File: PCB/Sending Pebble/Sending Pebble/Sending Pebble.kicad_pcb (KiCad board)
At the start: 4 copper layers, 50 x 50 mm, 48 parts, among them J1 USB_C_Receptacle_USB2.0_16P, J2 Conn_01x02_Socket, J3 u.Fl, J4 SMA, J5 Conn_01x02_Socket, Q1 IRLML0030, SW1 Boot, SW2 Reset, U1 LoRa-E5, U3 MAX-M10S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

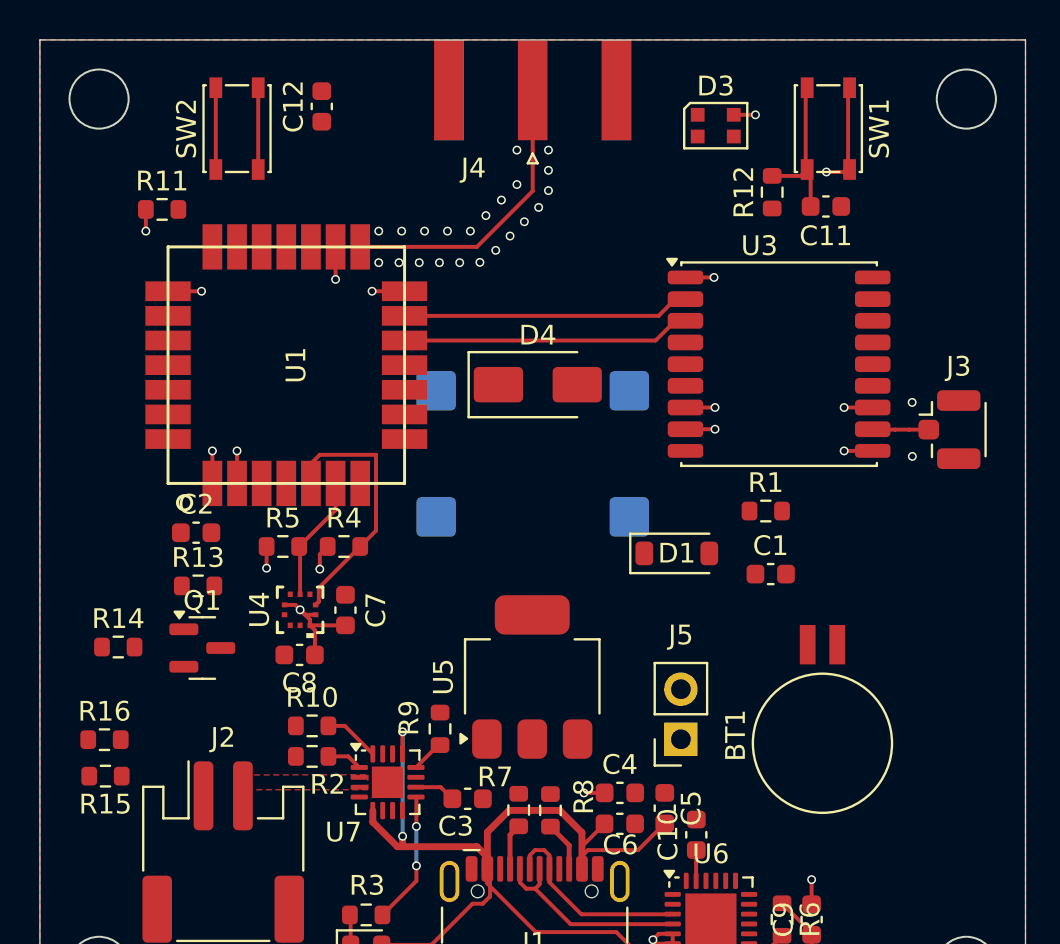
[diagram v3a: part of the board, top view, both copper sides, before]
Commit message: More layout and trace routing
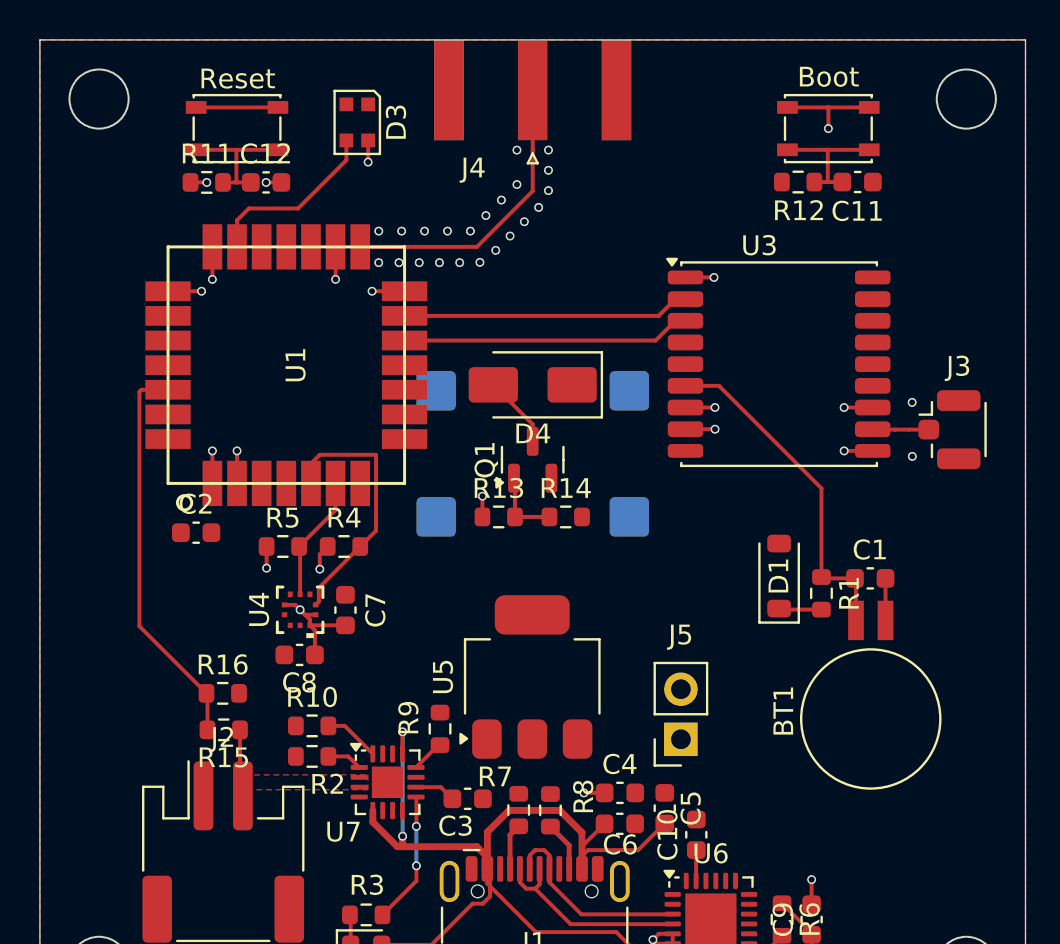
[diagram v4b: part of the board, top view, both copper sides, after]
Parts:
- moved R14 23.6 mm to (138.6, 81.8)
- moved Q1 19.3 mm to (136.9, 78.9), turned to 90 degrees
- moved D3 18.2 mm to (128.0, 61.8), turned to -90 degrees
- moved R13 15.6 mm to (135.2, 81.8)
- moved R15 6.44 mm to (121.2, 92.6)
- moved R16 6.44 mm to (121.2, 90.8)
- moved D1 5.32 mm to (149.4, 84.8), turned to 90 degrees
- moved C1 5.05 mm to (154.0, 84.9)
- moved R1 5.04 mm to (151.6, 85.7), turned to -90 degrees
- moved C12 4.78 mm to (123.4, 64.8), turned to 0 degrees
- moved BT1 2.74 mm to (154.1, 87.0)
- moved R11 2.65 mm to (120.4, 64.8)
- moved C11 2.03 mm to (153.4, 64.8)
- moved R12 1.41 mm to (150.4, 64.8), turned to 0 degrees
- moved D4 0.26 mm to (136.9, 75.1), turned to 180 degrees
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- renumbered SW1 to Boot, SW2 to Reset
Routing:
- net ADC: track 0.00 -> 20.1 mm
- net Net-(BT1-+): track 0.00 -> 17.4 mm
- net NEO: track 0.00 -> 9.16 mm
- net Net-(Q1-G): track 0.00 -> 3.73 mm
- net Net-(BZ1--): track 0.00 -> 3.69 mm
- net Net-(J2-Pin_2): track 0.00 -> 3.41 mm
- net RST: track 4.15 -> 7.22 mm
- net GND: track 16.4 -> 19.3 mm, vias 32 -> 33
- net BUZZ: track 0.00 -> 2.70 mm, vias 0 -> 2
- net Net-(D1-K): track 0.00 -> 2.17 mm
- net BOOT0: track 7.91 -> 7.21 mm

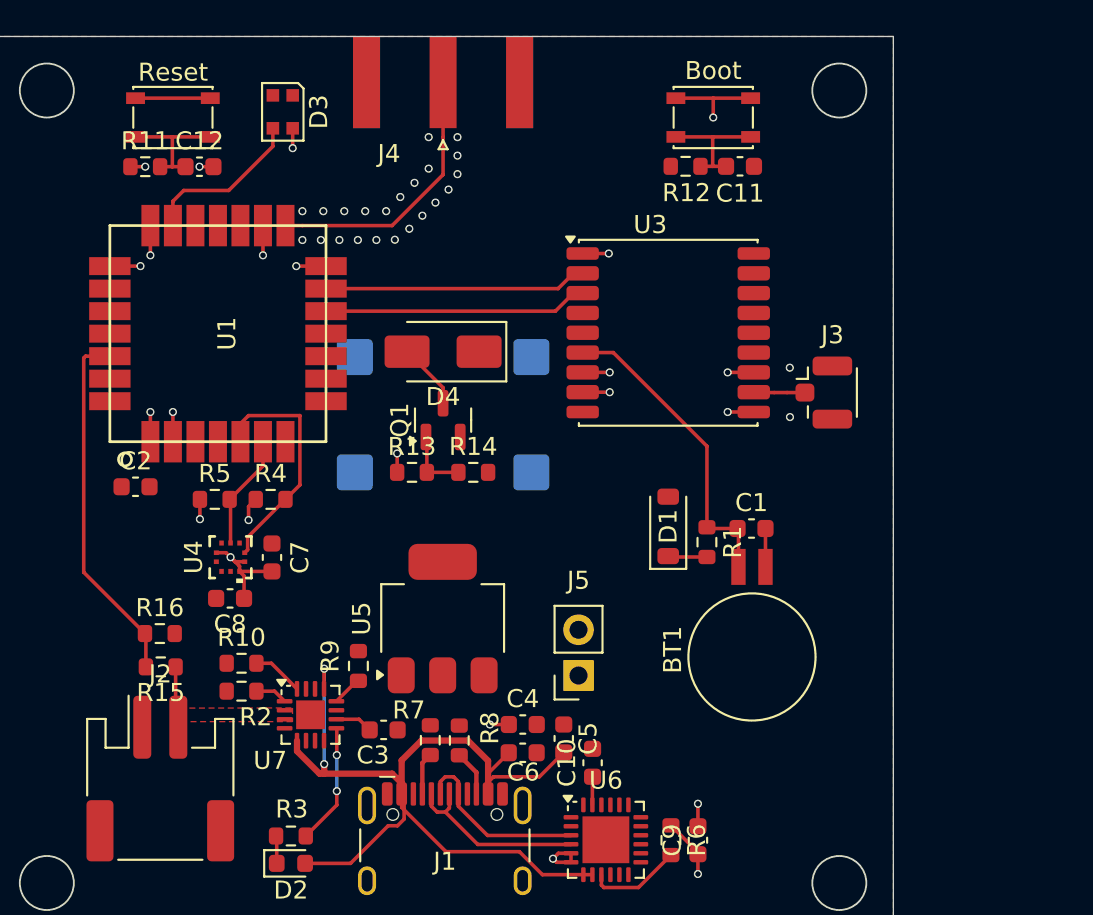
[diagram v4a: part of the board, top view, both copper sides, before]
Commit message: Fixed VREG type, more routing
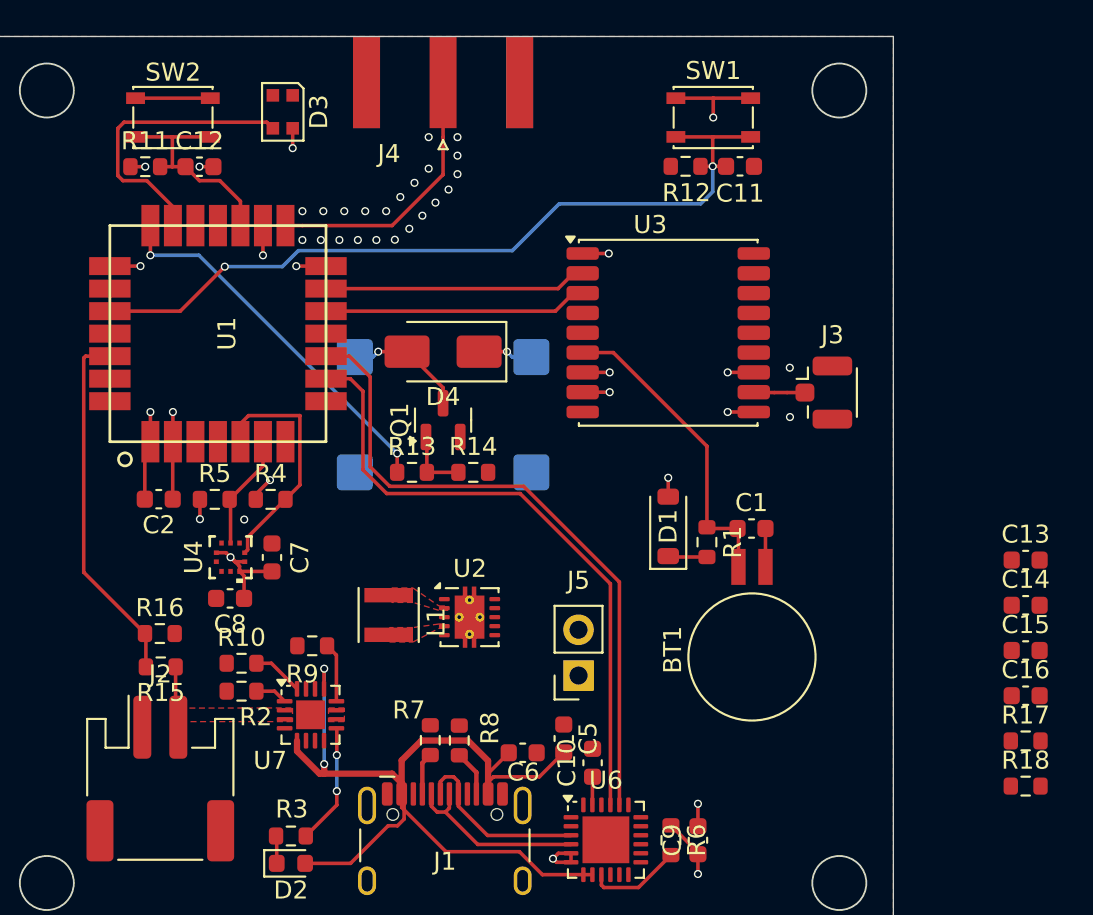
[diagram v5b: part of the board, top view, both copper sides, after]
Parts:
- removed C3: 10uF, Capacitor_SMD:C_0603_1608Metric
- removed C4: 22uF, Capacitor_SMD:C_0603_1608Metric
- removed U5: AZ1117CH2-3.3, Package_TO_SOT_SMD:SOT-223-3_TabPin2
- added C13: 10uF, Capacitor_SMD:C_0603_1608Metric, F.Cu at (169.2, 86.7)
- added C14: 10uF, Capacitor_SMD:C_0603_1608Metric, F.Cu at (169.2, 89.2)
- added C15: 0.1uF, Capacitor_SMD:C_0603_1608Metric, F.Cu at (169.2, 91.7)
- added C16: 10uF, Capacitor_SMD:C_0603_1608Metric, F.Cu at (169.2, 94.2)
- added L1: L, LQH3NPN2R2MMEL:IND_LQH3NPN2R2MMEL, F.Cu at (133.9, 89.7)
- added R17: 100, Resistor_SMD:R_0603_1608Metric, F.Cu at (169.2, 96.7)
- added R18: 10k, Resistor_SMD:R_0603_1608Metric, F.Cu at (169.2, 99.2)
- added U2: TPS63001, Package_SON:Texas_DRC0010J_ThermalVias, F.Cu at (138.4, 89.8)
- moved R9 2.80 mm to (129.6, 91.4), turned to 0 degrees
- moved C2 1.46 mm to (121.1, 83.3), turned to 180 degrees
- renumbered Boot to SW1, Reset to SW2
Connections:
- J5 pad 1: VBAT -> Net-(J5-Pin_1)
- J5 pad 2: Net-(J5-Pin_2) -> VBAT
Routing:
- net BOOT0: track 7.21 -> 44.8 mm, vias 0 -> 2
- net PB6/TX: track 0.00 -> 36.8 mm
- net PB7/RX: track 0.00 -> 35.3 mm
- net BUZZ: track 2.70 -> 21.0 mm
- net NEO: track 9.16 -> 16.3 mm
- net +3.3V: track 27.5 -> 33.9 mm, vias 12 -> 13
- net RST: track 7.22 -> 12.4 mm
- net GND: track 19.3 -> 22.5 mm, vias 33 -> 34
- net Net-(BZ1--): track 3.69 -> 6.72 mm, vias 0 -> 1
- net VBAT: track 2.11 -> 0.00 mm
- net Net-(U7-ILIM): track 1.69 -> 3.29 mm
- added copper zone on F.Cu, net Net-(U2-L1)
- added copper zone on F.Cu, net Net-(U2-L2)
- added copper zone on F.Cu, net VBAT

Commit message: More routing, added FC connection
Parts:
- moved C14 31.1 mm to (138.4, 85.5), turned to 180 degrees
- moved R17 31.1 mm to (138.4, 92.6)
- moved C13 30.9 mm to (138.4, 87.1), turned to 180 degrees
- moved C16 30.8 mm to (138.4, 94.2), turned to 180 degrees
- moved C15 27.7 mm to (141.6, 88.9), turned to 90 degrees
- moved R18 14.6 mm to (155.0, 96.5), turned to -90 degrees
- moved D3 14.1 mm to (115.0, 67.3), turned to 0 degrees
- moved PWR0 13.4 mm to (157.6, 95.6)
- moved R15 6.67 mm to (116.9, 87.5)
- moved R16 6.67 mm to (116.8, 85.7)
- moved J2 4.12 mm to (119.1, 95.2), turned to -90 degrees
- moved C1 3.73 mm to (151.4, 82.3)
- moved BT1 3.73 mm to (151.4, 84.4)
- moved D1 3.73 mm to (146.7, 82.2)
- moved R1 3.73 mm to (148.9, 83.1)
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- renumbered SW1 to BOOT, J5 to PWR0, SW2 to RESET
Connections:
- PWR0 pad 1: Net-(J5-Pin_1) -> EN
- R18 pad 1: Net-(J5-Pin_1) -> EN
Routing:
- net RST: track 12.4 -> 52.5 mm, vias 0 -> 2
- net VBAT: track 0.00 -> 23.7 mm, vias 0 -> 1
- net EN: track 0.00 -> 22.8 mm, vias 0 -> 1
- net NEO: track 16.3 -> 7.69 mm
- net Net-(J2-Pin_2): track 3.41 -> 11.5 mm
- net Net-(U2-PS/SYNC): track 0.00 -> 6.92 mm
- net ADC: track 20.1 -> 14.0 mm
- net +3.3V: track 33.9 -> 39.0 mm, vias 13 -> 15
- net GND: track 22.5 -> 26.7 mm, vias 34 -> 41
- net Net-(BT1-+): track 17.4 -> 14.1 mm
- net BOOT0: track 44.8 -> 42.1 mm
- net Net-(U7-TS): track 1.80 -> 3.71 mm
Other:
- outline, holes or cut-outs redrawn

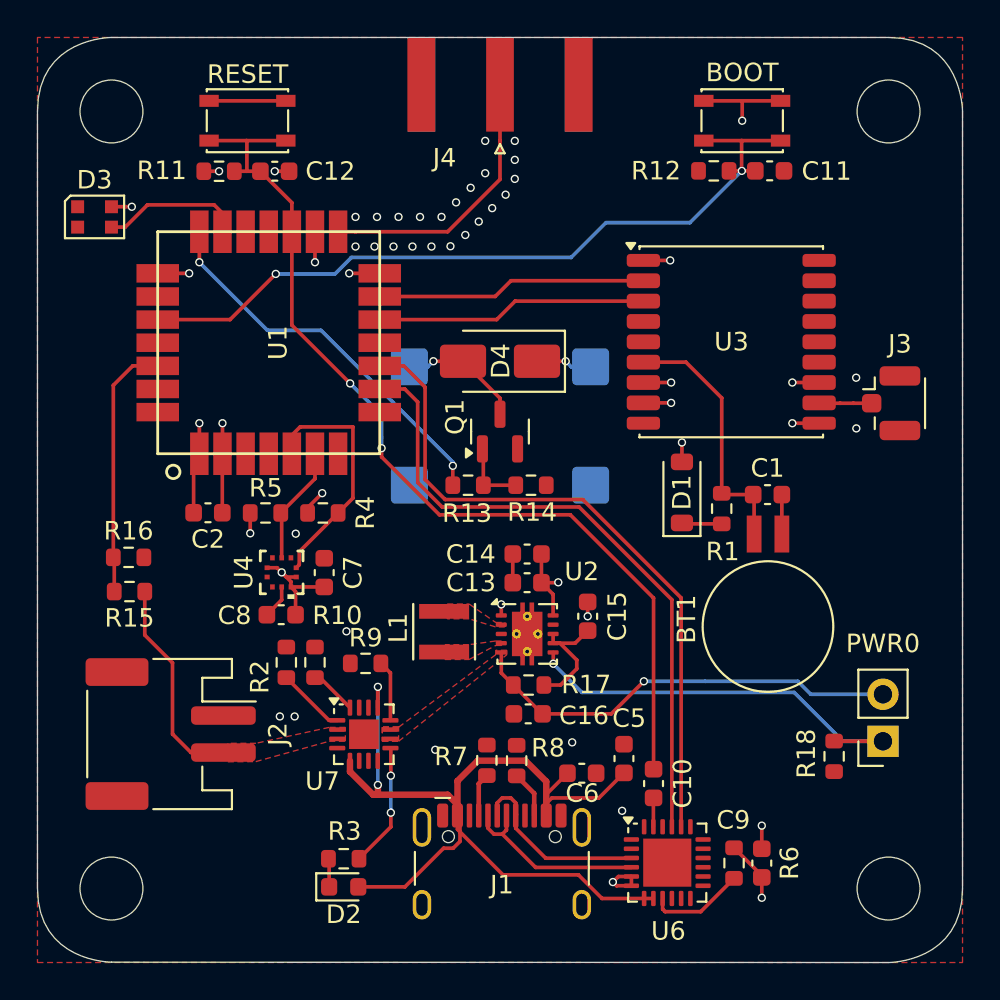
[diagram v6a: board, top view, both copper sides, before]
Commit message: More routing, added amplifier connector, fixed coplanar waveguide. Started adding graphics
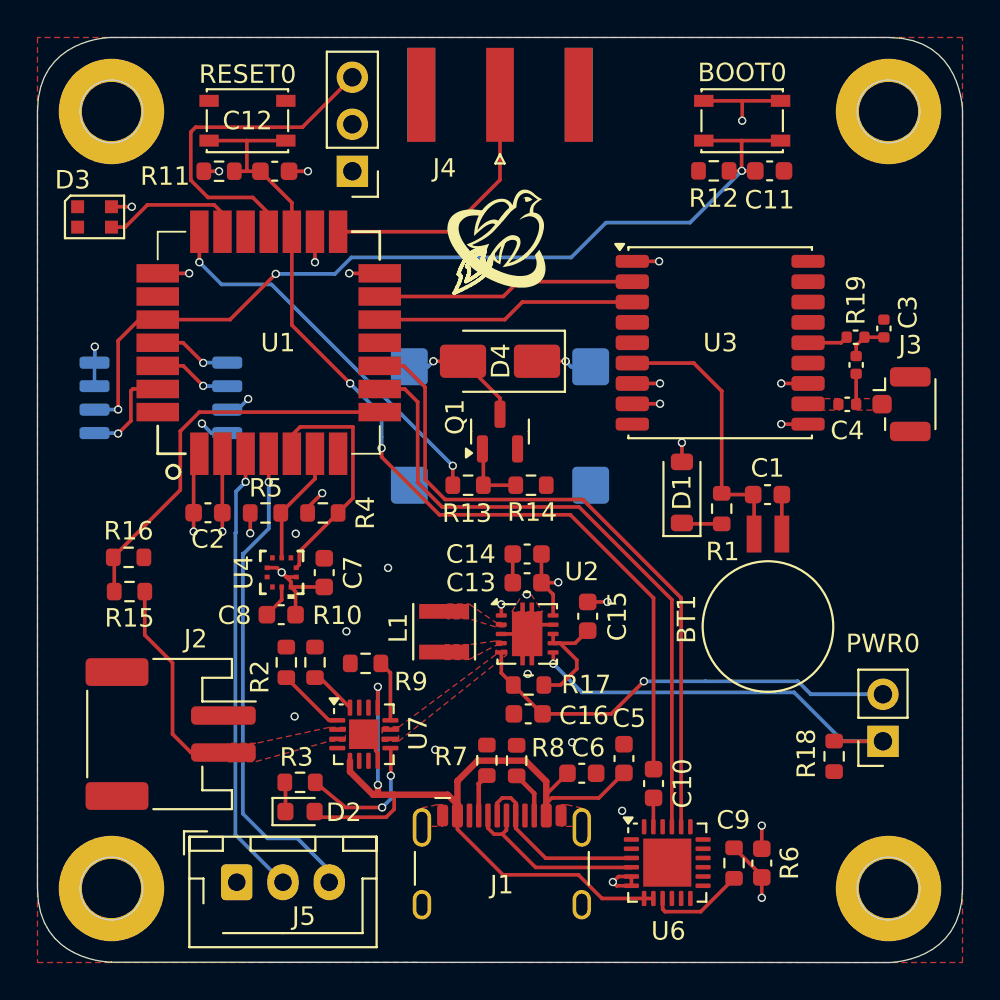
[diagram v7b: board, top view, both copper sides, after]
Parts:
- added C3: 10nF, Capacitor_SMD:C_0402_1005Metric, F.Cu at (157.7, 73.3)
- added C4: 47pF, Capacitor_SMD:C_0402_1005Metric, F.Cu at (155.7, 77.4)
- added G***: LOGO, Stone:stone_footprint, F.Cu at (169.6, 67.6)
- added J5: Conn_01x03_Socket, Connector_JST:JST_XH_B3B-XH-AM_1x03_P2.50mm_Vertical, F.Cu at (122.7, 103.3)
- added J6: Conn_01x03_Socket, Connector_PinHeader_2.54mm:PinHeader_1x03_P2.54mm_Vertical, F.Cu at (128.9, 64.8)
- added L2: 27nH, Capacitor_SMD:C_0402_1005Metric, F.Cu at (156.2, 75.3)
- added R19: 10, Capacitor_SMD:C_0402_1005Metric, F.Cu at (156.1, 73.8)
- added REF**: MountingHole_3.2mm_M3_ISO7380_Pad, MountingHole:MountingHole_3.2mm_M3_ISO7380_Pad, F.Cu at (115.9, 61.6)
- added REF**: MountingHole_3.2mm_M3_ISO7380_Pad, MountingHole:MountingHole_3.2mm_M3_ISO7380_Pad, F.Cu at (157.9, 61.6)
- added REF**: MountingHole_3.2mm_M3_ISO7380_Pad, MountingHole:MountingHole_3.2mm_M3_ISO7380_Pad, F.Cu at (115.9, 103.6)
- added REF**: MountingHole_3.2mm_M3_ISO7380_Pad, MountingHole:MountingHole_3.2mm_M3_ISO7380_Pad, F.Cu at (157.9, 103.6)
- added U5: W25Q32JVSS, Package_SO:SOIC-8_5.3x5.3mm_P1.27mm, B.Cu at (118.6, 77.1)
- moved R3 4.76 mm to (126.1, 97.9)
- moved D2 4.71 mm to (126.1, 99.4)
- moved U3 0.60 mm to (148.8, 74.1)
- moved J3 0.56 mm to (158.6, 77.4)
- moved J4 0.55 mm to (136.9, 60.7)
- renumbered BOOT to BOOT0, RESET to RESET0
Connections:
- U1 pad 18: unconnected-(U1-PA3-Pad18) -> AMP
- U1 pad 25: unconnected-(U1-PB9-Pad25) -> NSS
- U1 pad 26: ADC -> MISO
- U1 pad 27: unconnected-(U1-PA10-Pad27) -> MOSI
- U1 pad 3: unconnected-(U1-PA13-Pad3) -> FC-TX
- U1 pad 4: unconnected-(U1-PA14-Pad4) -> FC-RX
- U1 pad 8: unconnected-(U1-PB3-Pad8) -> ADC
- U3 pad 11: Net-(J3-In) -> Net-(U3-RF_IN)
- U3 pad 14: unconnected-(U3-VCC_RF-Pad14) -> Net-(U3-VCC_RF)
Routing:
- net FC-RX: track 0.00 -> 26.6 mm, vias 0 -> 1
- net FC-TX: track 0.00 -> 24.5 mm, vias 0 -> 1
- net AMP: track 0.00 -> 18.5 mm
- net BOOT0: track 42.1 -> 49.7 mm, vias 2 -> 3
- net ADC: track 14.0 -> 21.4 mm
- net MOSI: track 0.00 -> 5.38 mm, vias 0 -> 1
- net NSS: track 0.00 -> 4.22 mm, vias 0 -> 1
- net MISO: track 0.00 -> 4.21 mm, vias 0 -> 1
- net +3.3V: track 39.0 -> 41.9 mm, vias 15 -> 17
- net VBUS: track 53.3 -> 50.7 mm
- net Net-(C3-Pad1): track 0.00 -> 2.26 mm
- net Net-(U3-VCC_RF): track 0.00 -> 2.21 mm
- net GND: track 26.7 -> 28.8 mm, vias 41 -> 20
- net Net-(J3-In): track 2.88 -> 1.65 mm
- net Net-(U7-~{CHG}): track 6.70 -> 7.52 mm
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- added copper zone on F.Cu, net Net-(J3-In)
- added copper zone on F.Cu, net Net-(U3-RF_IN)

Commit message: Finished RF design, added finished graphics, added pin labels
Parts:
- moved G*** 28.1 mm to (150.3, 88.0)
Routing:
- net GND: track 28.8 -> 25.9 mm, vias 20 -> 85
- net BOOT0: track 49.7 -> 50.3 mm
- added copper zone on B.Cu, net (none)
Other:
- board text added: "+"
- board text added: "-"
- board text added: "3.3"
- board text added: "EN"
- board text added: "GND"
- board text added: "RX"
- board text added: "Sending Pebble"
- board text added: "TX"
- board text added: "Telemetry"
